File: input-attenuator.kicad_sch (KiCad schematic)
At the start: 86 parts, among them J1 DC_INTF, J2 DC_INTF, J3 RX_1_RF, J4 RX_2_RF, J5 RF_IN, K1 EE2-5TNU-L, K2 EE2-5TNU-L, K3 EE2-5TNU-L, K4 EE2-5TNU-L, Q1 BC858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

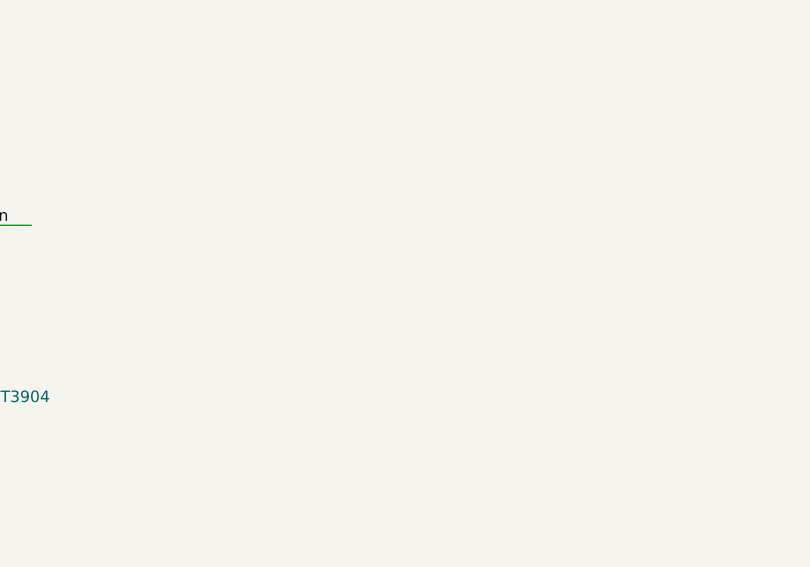
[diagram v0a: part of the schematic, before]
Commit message: Added edge cuts, mounting holes and improved silkscreen
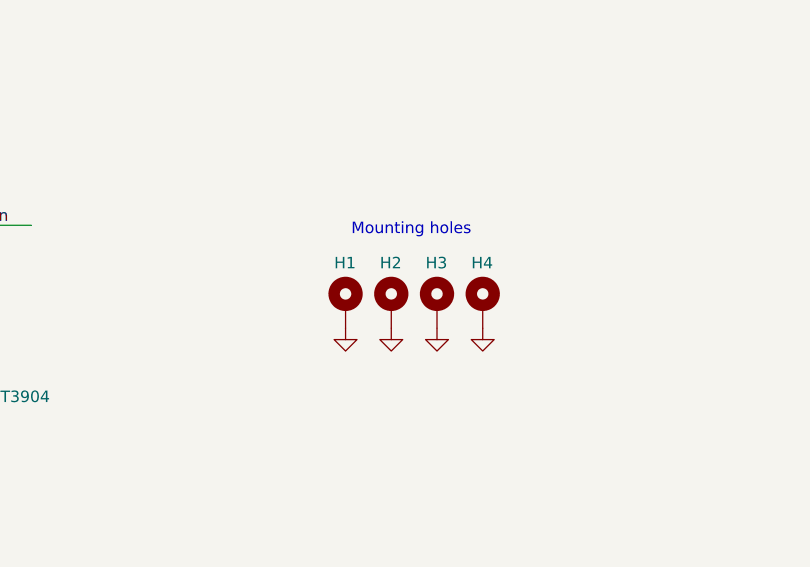
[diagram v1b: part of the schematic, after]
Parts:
- added H1, H2, H3, H4: MountingHole_Pad, MountingHole:MountingHole_3.2mm_M3_ISO7380_Pad, symbol Mechanical:MountingHole_Pad
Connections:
- net GND: now also H1.1, H2.1, H3.1, H4.1
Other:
- note added: "Mounting holes"
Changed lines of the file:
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@@
     (effects (font (size 1.27 1.27)) (justify left bottom))
+  )
+  (text "Mounting holes" (at 241.3 128.27 180)
+    (effects (font (size 1.27 1.27)) (justify right bottom))
   )
   (label "SHDN" (at 20.32 167.64 0)
@@
     (pin "1")
   )
+  (symbol (lib_id "power:GND") (at 227.33 138.43 0) (unit 1)
+    (in_bom yes) (on_board yes)
+    (property "Reference" "#PWR02" (id 0) (at 227.33 144.78 0)
+      (effects (font (size 1.27 1.27)) hide)
+    )
+    (property "Value" "GND" (id 1) (at 227.457 142.9258 0)
+      (effects (font (size 1.27 1.27)) hide)
+    )
+    (property "Footprint" "" (id 2) (at 227.33 138.43 0)
+      (effects (font (size 1.27 1.27)) hide)
+    )
+    (property "Datasheet" "" (id 3) (at 227.33 138.43 0)
+      (effects (font (size 1.27 1.27)) hide)
+    )
+    (pin "1")
+  )
   (symbol (lib_id "power:GND") (at 229.235 38.1 180) (unit 1)
     (in_bom yes) (on_board yes)
@@
     (pin "1")
   )
+  (symbol (lib_id "power:GND") (at 232.41 138.43 0) (unit 1)
+    (in_bom yes) (on_board yes)
+    (property "Reference" "#PWR03" (id 0) (at 232.41 144.78 0)
+      (effects (font (size 1.27 1.27)) hide)
+    )
+    (property "Value" "GND" (id 1) (at 232.537 142.9258 0)
+      (effects (font (size 1.27 1.27)) hide)
+    )
+    (property "Footprint" "" (id 2) (at 232.41 138.43 0)
+      (effects (font (size 1.27 1.27)) hide)
+    )
+    (property "Datasheet" "" (id 3) (at 232.41 138.43 0)
+      (effects (font (size 1.27 1.27)) hide)
+    )
+    (pin "1")
+  )
   (symbol (lib_id "power:GND") (at 233.045 95.885 270) (unit 1)
     (in_bom yes) (on_board yes)
@@
     )
     (property "Datasheet" "" (id 3) (at 233.045 95.885 0)
+      (effects (font (size 1.27 1.27)) hide)
+    )
+    (pin "1")
+  )
+  (symbol (lib_id "power:GND") (at 237.49 138.43 0) (unit 1)
+    (in_bom yes) (on_board yes)
+    (property "Reference" "#PWR04" (id 0) (at 237.49 144.78 0)
+      (effects (font (size 1.27 1.27)) hide)
+    )
+    (property "Value" "GND" (id 1) (at 237.617 142.9258 0)
+      (effects (font (size 1.27 1.27)) hide)
+    )
+    (property "Footprint" "" (id 2) (at 237.49 138.43 0)
+      (effects (font (size 1.27 1.27)) hide)
+    )
+    (property "Datasheet" "" (id 3) (at 237.49 138.43 0)
+      (effects (font (size 1.27 1.27)) hide)
+    )
+    (pin "1")
+  )
+  (symbol (lib_id "power:GND") (at 242.57 138.43 0) (unit 1)
+    (in_bom yes) (on_board yes)
+    (property "Reference" "#PWR05" (id 0) (at 242.57 144.78 0)
+      (effects (font (size 1.27 1.27)) hide)
+    )
+    (property "Value" "GND" (id 1) (at 242.697 142.9258 0)
+      (effects (font (size 1.27 1.27)) hide)
+    )
+    (property "Footprint" "" (id 2) (at 242.57 138.43 0)
+      (effects (font (size 1.27 1.27)) hide)
+    )
+    (property "Datasheet" "" (id 3) (at 242.57 138.43 0)
       (effects (font (size 1.27 1.27)) hide)
     )
@@
     (pin "2")
   )
+  (symbol (lib_id "Comparator:LM339") (at 149.225 172.085 0) (unit 5)
+    (in_bom yes) (on_board yes)
+    (property "Reference" "U8" (id 0) (at 149.225 162.7948 0))
+    (property "Value" "LP339" (id 1) (at 149.225 165.093 0))
+    (property "Footprint" "Package_SO:SO-14_3.9x8.65mm_P1.27mm" (id 2) (at 147.955 169.545 0)
+      (effects (font (size 1.27 1.27)) hide)
+    )
+    (property "Datasheet" "https://www.st.com/resource/en/datasheet/lm139.pdf" (id 3) (at 150.495 167.005 0)
+      (effects (font (size 1.27 1.27)) hide)
+    )
+    (pin "12")
+    (pin "3")
+  )
   (symbol (lib_id "Device:D_Small_ALT") (at 29.21 49.53 270) (mirror x) (unit 1)
     (in_bom yes) (on_board yes)
@@
     (pin "2")
   )
-  (symbol (lib_id "Comparator:LM339") (at 149.225 172.085 0) (unit 5)
-    (in_bom yes) (on_board yes)
-    (property "Reference" "U8" (id 0) (at 149.225 162.7948 0))
-    (property "Value" "LP339" (id 1) (at 149.225 165.093 0))
-    (property "Footprint" "Package_SO:SO-14_3.9x8.65mm_P1.27mm" (id 2) (at 147.955 169.545 0)
-      (effects (font (size 1.27 1.27)) hide)
-    )
-    (property "Datasheet" "https://www.st.com/resource/en/datasheet/lm139.pdf" (id 3) (at 150.495 167.005 0)
-      (effects (font (size 1.27 1.27)) hide)
-    )
-    (pin "12")
-    (pin "3")
+  (symbol (lib_id "Mechanical:MountingHole_Pad") (at 227.33 135.89 0) (unit 1)
+    (in_bom yes) (on_board yes)
+    (property "Reference" "H1" (id 0) (at 226.0601 131.1921 0)
+      (effects (font (size 1.27 1.27)) (justify left))
+    )
+    (property "Value" "MountingHole_Pad" (id 1) (at 229.8701 137.3008 0)
+      (effects (font (size 1.27 1.27)) (justify left) hide)
+    )
+    (property "Footprint" "MountingHole:MountingHole_3.2mm_M3_ISO7380_Pad" (id 2) (at 227.33 135.89 0)
+      (effects (font (size 1.27 1.27)) hide)
+    )
+    (property "Datasheet" "~" (id 3) (at 227.33 135.89 0)
+      (effects (font (size 1.27 1.27)) hide)
+    )
+    (pin "1")
+  )
+  (symbol (lib_id "Mechanical:MountingHole_Pad") (at 232.41 135.89 0) (unit 1)
+    (in_bom yes) (on_board yes)
+    (property "Reference" "H2" (id 0) (at 231.1401 131.1921 0)
+      (effects (font (size 1.27 1.27)) (justify left))
+    )
+    (property "Value" "MountingHole_Pad" (id 1) (at 234.9501 137.3008 0)
+      (effects (font (size 1.27 1.27)) (justify left) hide)
+    )
+    (property "Footprint" "MountingHole:MountingHole_3.2mm_M3_ISO7380_Pad" (id 2) (at 232.41 135.89 0)
+      (effects (font (size 1.27 1.27)) hide)
+    )
+    (property "Datasheet" "~" (id 3) (at 232.41 135.89 0)
+      (effects (font (size 1.27 1.27)) hide)
+    )
+    (pin "1")
+  )
+  (symbol (lib_id "Mechanical:MountingHole_Pad") (at 237.49 135.89 0) (unit 1)
+    (in_bom yes) (on_board yes)
+    (property "Reference" "H3" (id 0) (at 236.2201 131.1921 0)
+      (effects (font (size 1.27 1.27)) (justify left))
+    )
+    (property "Value" "MountingHole_Pad" (id 1) (at 240.0301 137.3008 0)
+      (effects (font (size 1.27 1.27)) (justify left) hide)
+    )
+    (property "Footprint" "MountingHole:MountingHole_3.2mm_M3_ISO7380_Pad" (id 2) (at 237.49 135.89 0)
+      (effects (font (size 1.27 1.27)) hide)
+    )
+    (property "Datasheet" "~" (id 3) (at 237.49 135.89 0)
+      (effects (font (size 1.27 1.27)) hide)
+    )
+    (pin "1")
+  )
+  (symbol (lib_id "Mechanical:MountingHole_Pad") (at 242.57 135.89 0) (unit 1)
+    (in_bom yes) (on_board yes)
+    (property "Reference" "H4" (id 0) (at 241.3001 131.1921 0)
+      (effects (font (size 1.27 1.27)) (justify left))
+    )
+    (property "Value" "MountingHole_Pad" (id 1) (at 245.1101 137.3008 0)
+      (effects (font (size 1.27 1.27)) (justify left) hide)
+    )
+    (property "Footprint" "MountingHole:MountingHole_3.2mm_M3_ISO7380_Pad" (id 2) (at 242.57 135.89 0)
+      (effects (font (size 1.27 1.27)) hide)
+    )
+    (property "Datasheet" "~" (id 3) (at 242.57 135.89 0)
+      (effects (font (size 1.27 1.27)) hide)
+    )
+    (pin "1")
   )
   (symbol (lib_id "Connector:Conn_Coaxial") (at 19.685 32.385 0) (mirror y) (unit 1)
@@
       (reference "#PWR01") (unit 1) (value "GND") (footprint "")
     )
+    (path "/9d7a6342-a602-4cc3-aab7-9b47fcdf1836"
+      (reference "#PWR02") (unit 1) (value "GND") (footprint "")
+    )
+    (path "/c26cad72-5351-4214-aee7-ac9e87bef845"
+      (reference "#PWR03") (unit 1) (value "GND") (footprint "")
+    )
+    (path "/99cdf0d8-c309-412d-9aed-7508ba2a62c3"
+      (reference "#PWR04") (unit 1) (value "GND") (footprint "")
+    )
+    (path "/2504a77b-f274-460b-9c54-3a7410a03e18"
+      (reference "#PWR05") (unit 1) (value "GND") (footprint "")
+    )
     (path "/00000000-0000-0000-0000-00005f2fde24"
       (reference "#PWR06") (unit 1) (value "GND") (footprint "")
@@
       (reference "D10") (unit 1) (value "S1BB") (footprint "Diode_SMD:D_SMB_Handsoldering")
     )
+    (path "/a629dcd5-83ba-4ebe-ad3c-5c1f6cfd9ad9"
+      (reference "H1") (unit 1) (value "MountingHole_Pad") (footprint "MountingHole:MountingHole_3.2mm_M3_ISO7380_Pad")
+    )
+    (path "/c04815fb-2e6d-4634-918c-1b95ead7976a"
+      (reference "H2") (unit 1) (value "MountingHole_Pad") (footprint "MountingHole:MountingHole_3.2mm_M3_ISO7380_Pad")
+    )
+    (path "/f8c31f98-d238-4aa8-93f0-b72e08897b30"
+      (reference "H3") (unit 1) (value "MountingHole_Pad") (footprint "MountingHole:MountingHole_3.2mm_M3_ISO7380_Pad")
+    )
+    (path "/d0a5d19a-fafc-47c2-b57c-cb2407bfc363"
+      (reference "H4") (unit 1) (value "MountingHole_Pad") (footprint "MountingHole:MountingHole_3.2mm_M3_ISO7380_Pad")
+    )
     (path "/92e7aac3-ac59-4653-8577-27b028dac29e"

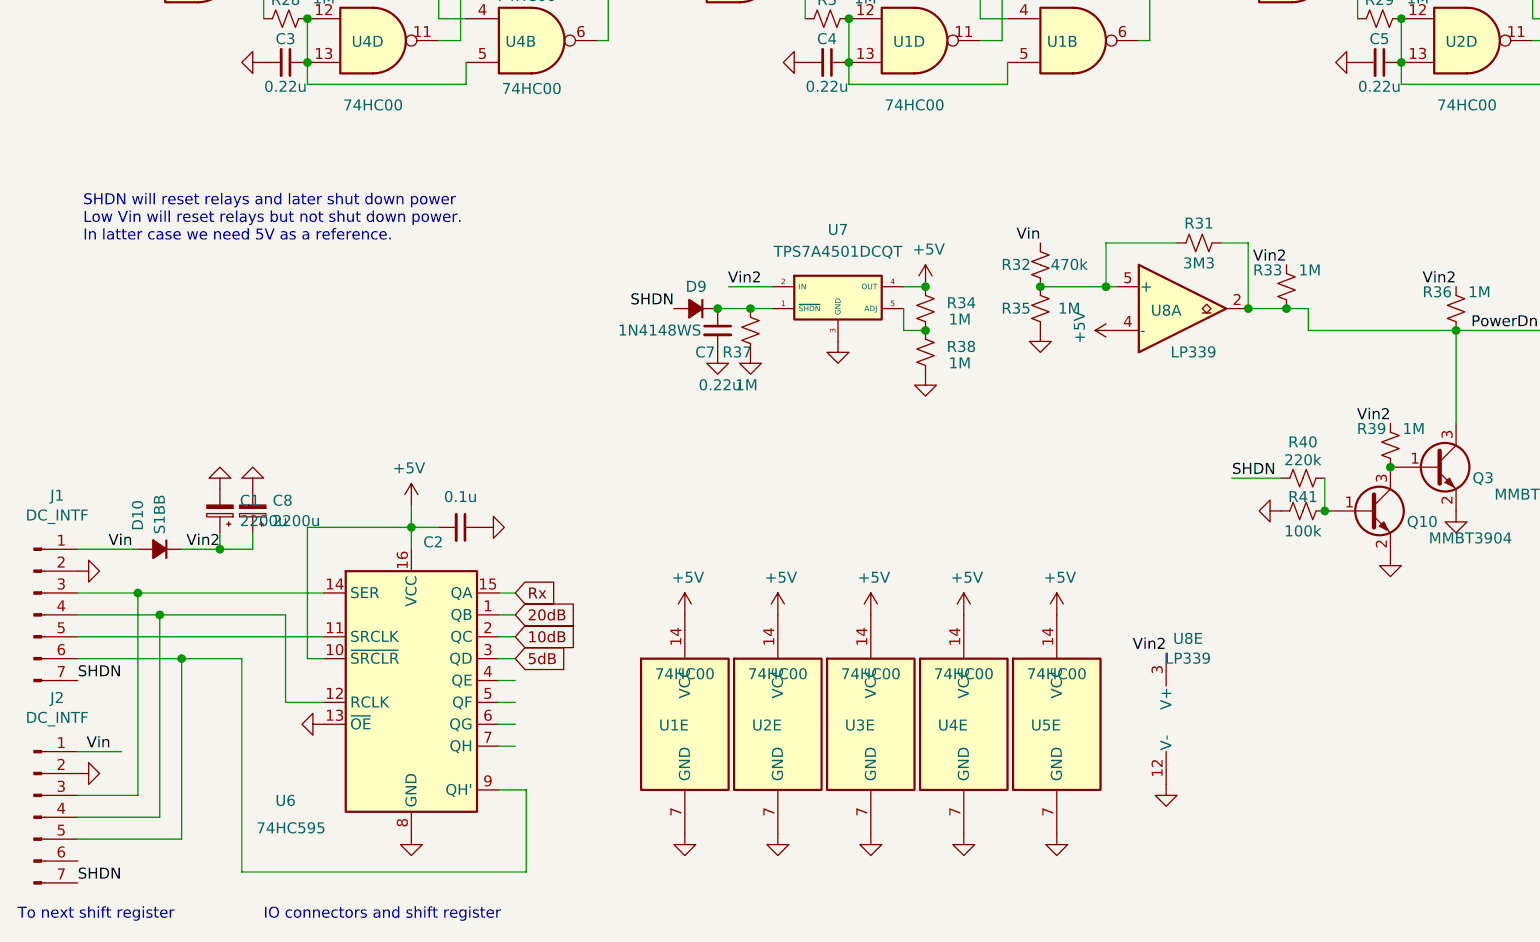
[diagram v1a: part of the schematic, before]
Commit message: Schema: added inrush resistors, made ERC pass, updated old symbols
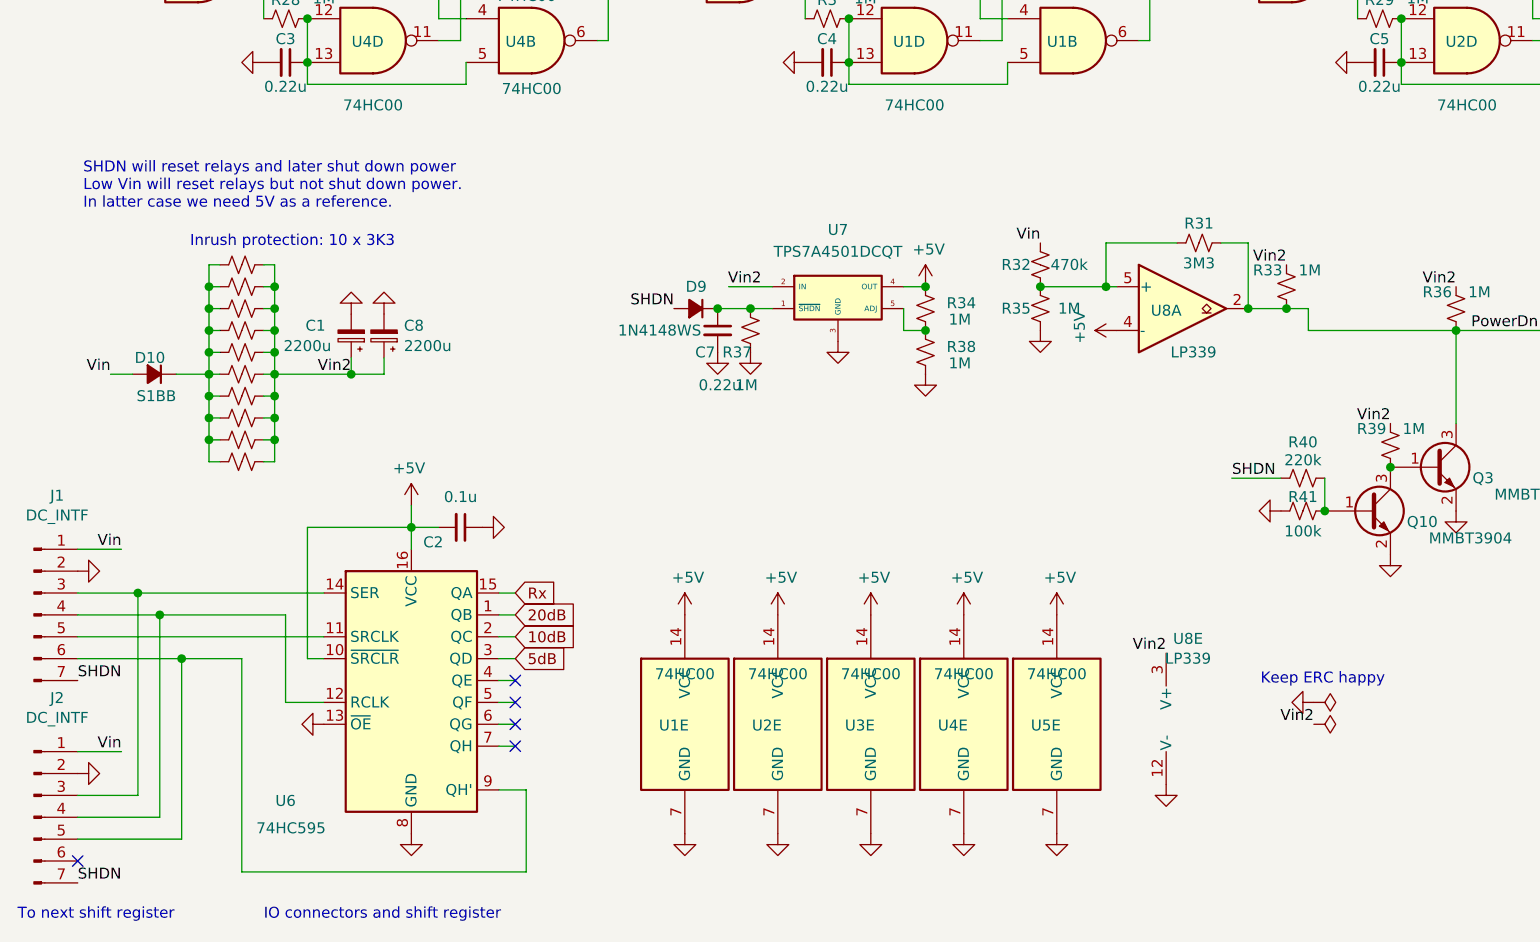
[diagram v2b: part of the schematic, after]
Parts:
- added R42, R43, R44, R45, R46, R47, R48, R49, R50, R51: 3K3, Resistor_SMD:R_0805_2012Metric, symbol Device:R_Small_US
- C1, C8: symbol Device:CP_Small -> Device:C_Polarized_Small
- D1, D10, D2, D3, D4, D5, D6, D7, D8, D9: symbol Device:D_Small_ALT -> Device:D_Small_Filled
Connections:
- net Vin2: now also R42.2, R43.2, R44.2, R45.2, R46.2, R47.2, R48.2, R49.2, R50.2, R51.2; no longer D10.1 (K)
- new net: D10.1 (K), R42.1, R43.1, R44.1, R45.1, R46.1, R47.1, R48.1, R49.1, R50.1, R51.1
- no-connect marks 0 -> 5
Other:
- note added: "Inrush protection: 10 x 3K3"
- note added: "Keep ERC happy"
- moved on the sheet: C1, C8, D10
